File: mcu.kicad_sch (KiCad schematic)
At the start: 17 parts, among them J4 Conn_01x04, Q1 RE1C002UNTCL, SW1 EVQP7A01P, SW2 EVQP7A01P, U2 TXB0304RUTR, U8 MX25L3233FM2I-08G, U9 ESP32-S3-WROOM-1-N16R8

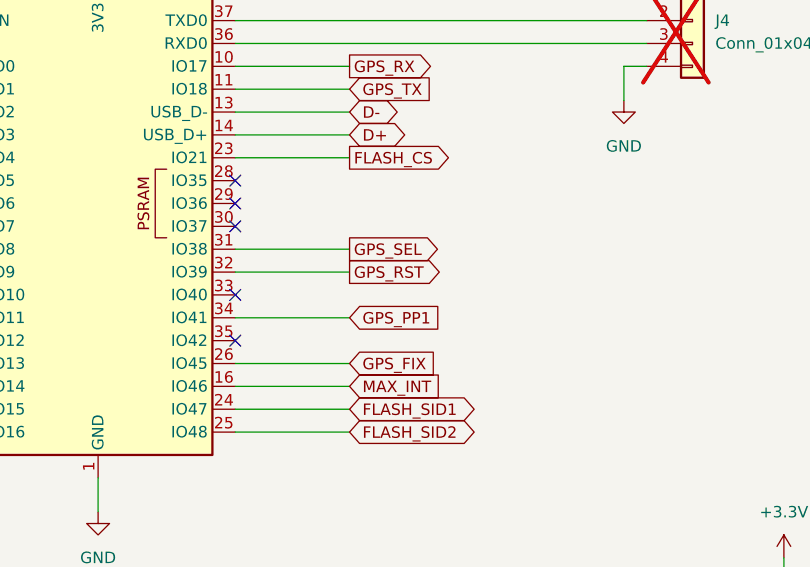
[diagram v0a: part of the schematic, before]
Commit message: reduce board size
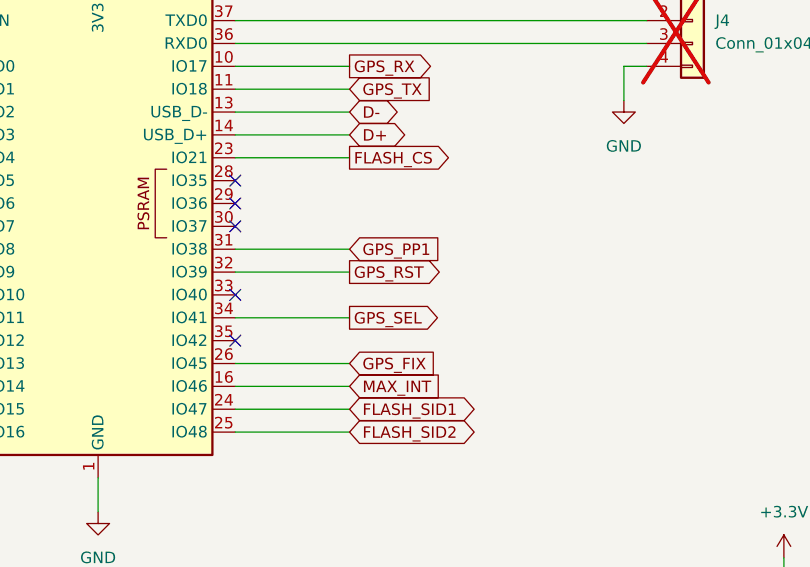
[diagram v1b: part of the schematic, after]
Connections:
- net GPS_PP1: now also U9.31 (IO38); no longer U9.34 (IO41)
- net GPS_SEL: now also U9.34 (IO41); no longer U9.31 (IO38)
